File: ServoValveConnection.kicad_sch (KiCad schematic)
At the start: 17 parts, among them J5 Valve, U1 ZXBM5210-SP

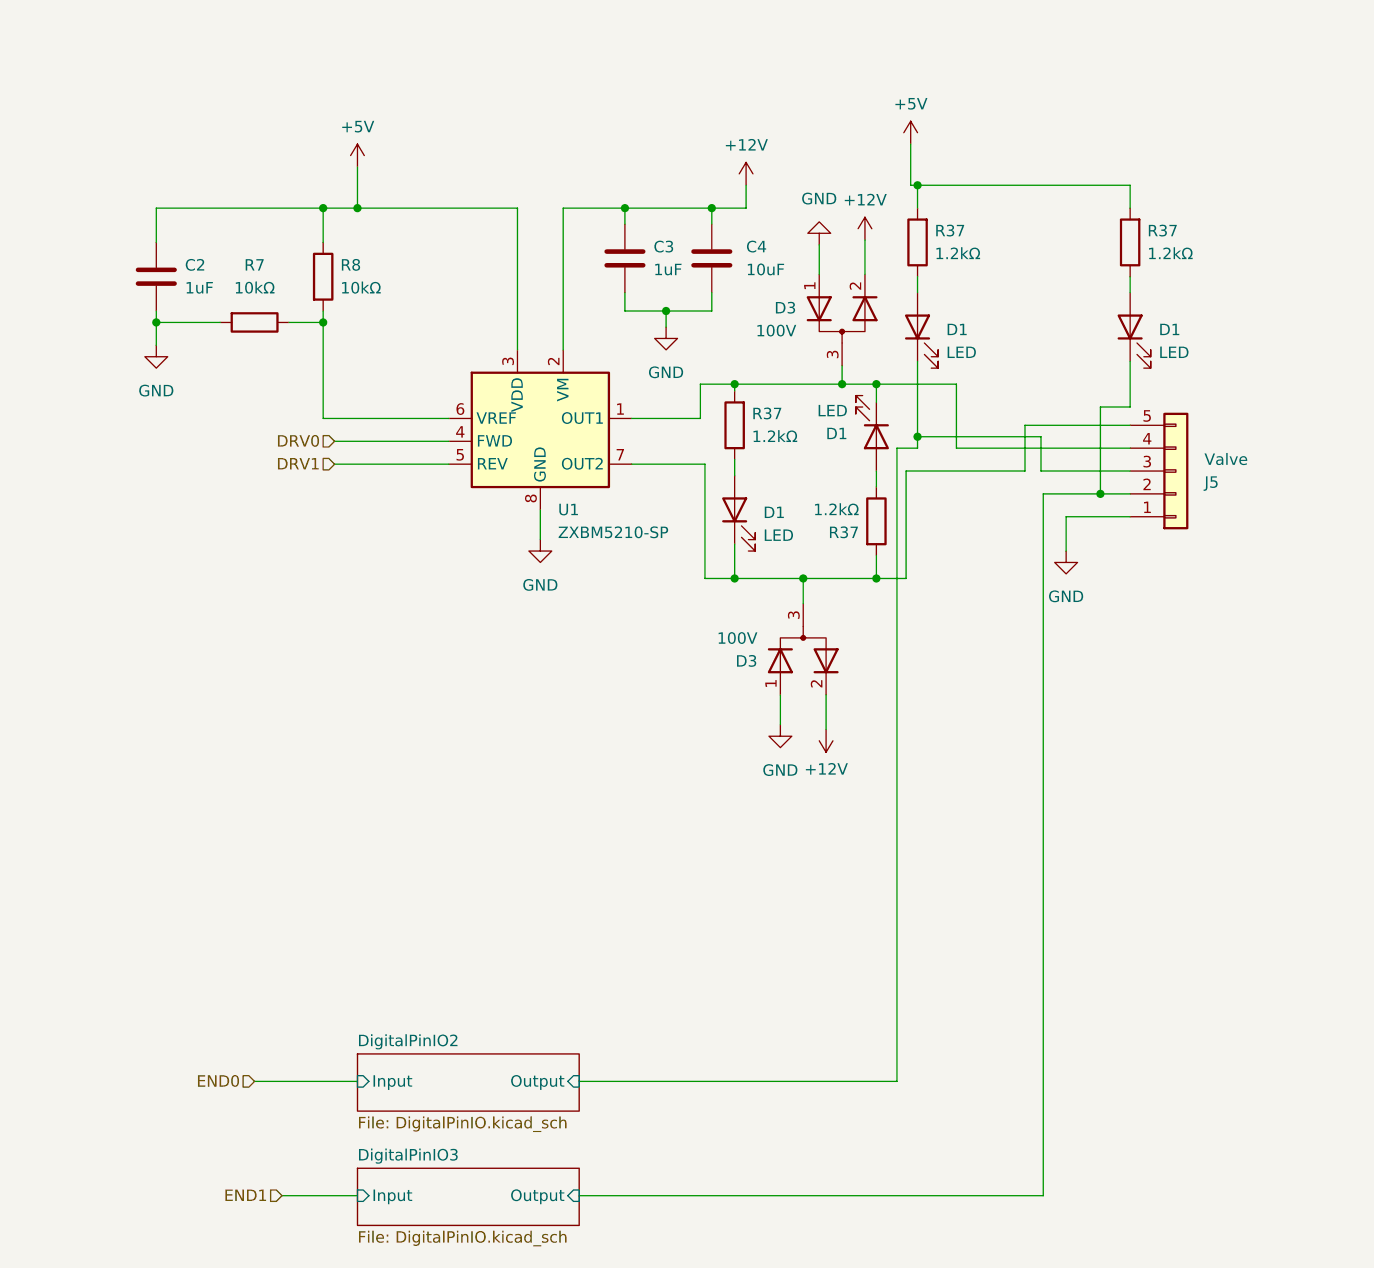
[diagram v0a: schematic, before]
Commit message: Updated gate driver to BD6222 since the old one did not have enough current.
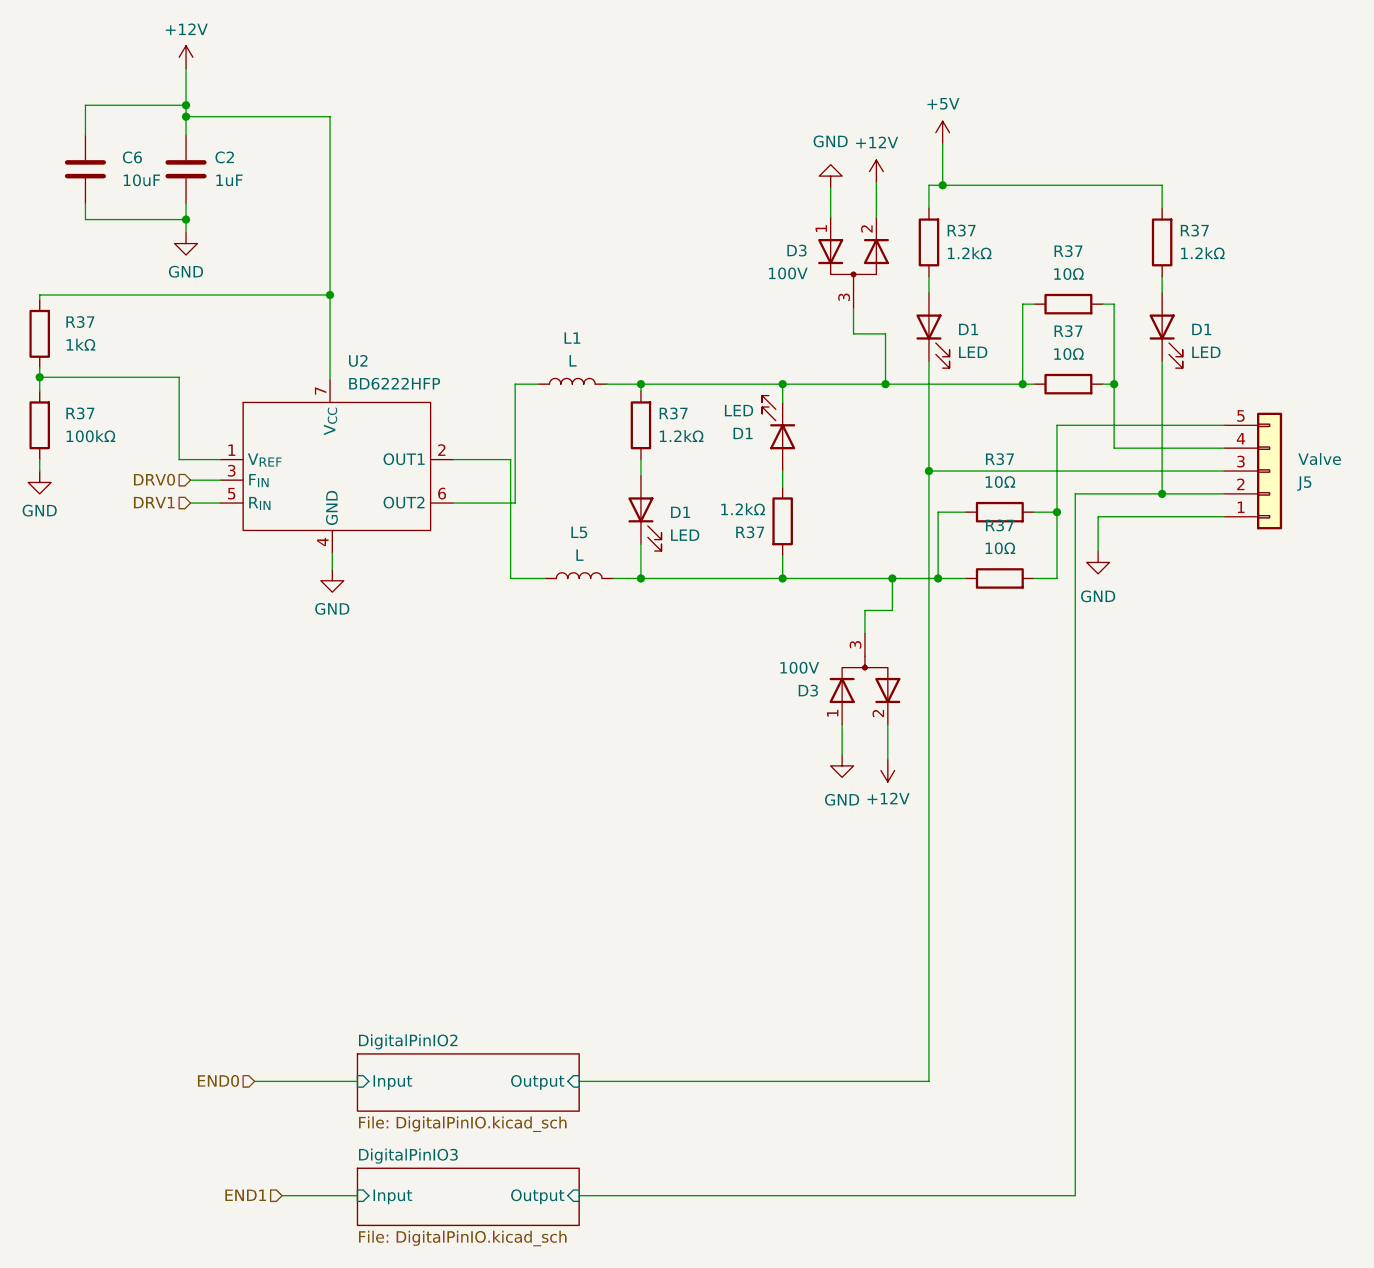
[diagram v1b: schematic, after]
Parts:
- removed C3: 1uF, Capacitor_SMD:C_0805_2012Metric, symbol Device:C
- removed C4: 10uF, Capacitor_SMD:C_0805_2012Metric, symbol Device:C
- removed R7, R8: 10kΩ, Resistor_SMD:R_0805_2012Metric, symbol Device:R
- removed U1: ZXBM5210-SP, Package_SO:Diodes_SO-8EP, symbol Driver_Motor:ZXBM5210-SP
- added C6: 10uF, Capacitor_SMD:C_0805_2012Metric, symbol Device:C
- added L1, L5: L, Inductor_SMD:L_Bourns-SRN4018, symbol Device:L
- added R37 (x4): 10Ω, Resistor_SMD:R_0805_2012Metric, symbol Device:R
- added R37: 1kΩ, Resistor_SMD:R_0805_2012Metric, symbol Device:R
- added R37: 100kΩ, Resistor_SMD:R_0805_2012Metric, symbol Device:R
- added U2: BD6222HFP, Package_TO_SOT_SMD:Rohm_HRP7, symbol FullBridgeDriver:BD6222HFP
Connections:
- net +12V: now also C2.1, C6.1, R37.2, U2.7 (V_{CC})
- net +5V: no longer C2.1
- net DRV0: now also U2.3 (F_{IN})
- net DRV1: now also U2.5 (R_{IN})
- net GND: now also C6.2, R37.1, U2.4 (GND)
- net at D1.1 (K), D3.3 (A), R37.2: now also L5.2, R37.1, R37.1; no longer J5.5 (Pin_5)
- net at D1.1 (K), D3.3 (A), R37.2: now also L1.2, R37.1, R37.1; no longer J5.4 (Pin_4)
- new net: J5.5 (Pin_5), R37.2, R37.2
- new net: L5.1, U2.2 (OUT1)
- new net: R37.1, R37.2, U2.1 (V_{REF})
- new net: J5.4 (Pin_4), R37.2, R37.2
- new net: L1.1, U2.6 (OUT2)
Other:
- moved on the sheet: D1, D3, J5, R37
